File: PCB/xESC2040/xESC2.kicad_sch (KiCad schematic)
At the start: 52 parts, among them J1 Conn_01x06_Male, J2 U254-051T-4BH83-F1S, J3 Conn_01x05_Male, J4 Conn_01x05_Male, J5 Conn_01x03_Male, U1 SN65HVD232

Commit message: WIP new power stage
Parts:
- removed C1, C10, C4, C7, C8, C9: DNP, Capacitor_SMD:C_0603_1608Metric, symbol Device:C
- removed R1, R10, R14, R17, R19, R4: 1k5, Resistor_SMD:R_0603_1608Metric, symbol Device:R
- removed R11, R2, R5: 2k2, Resistor_SMD:R_0603_1608Metric, symbol Device:R
- removed R13, R16, R18: 22k, Resistor_SMD:R_0603_1608Metric, symbol Device:R
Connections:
- net MCU/MISO_EXT renamed MCU/SHUTDOWN
- net MCU/RX_NCS_EXT renamed MCU/UART_RX
- net MCU/SCK_EXT: no longer names the net of J4.3 (Pin_3)
- net MCU/TX_MOSI_EXT renamed MCU/UART_TX
- no-connect marks 1 -> 2
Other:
- sheet MCU ports: added CURRENT_SENSE, SHUTDOWN, UART_RX, UART_TX; removed CUR_U, CUR_V, CUR_W, DRV_ENABLE, DRV_MISO, DRV_MOSI, DRV_NCS, DRV_SCK, FAULT, MISO_EXT, PHASE_U, PHASE_V, PHASE_W, RX_NCS_EXT, SCK_EXT, SERVO, TX_MOSI_EXT
- sheet Power ports: added CUR_SENSE; removed CURU_5V, CURV_5V, CURW_5V, DRV_ENABLE, FAULT, MISO, MOSI, NCS, PHASE_U, PHASE_V, PHASE_W, SCK, VCCIO

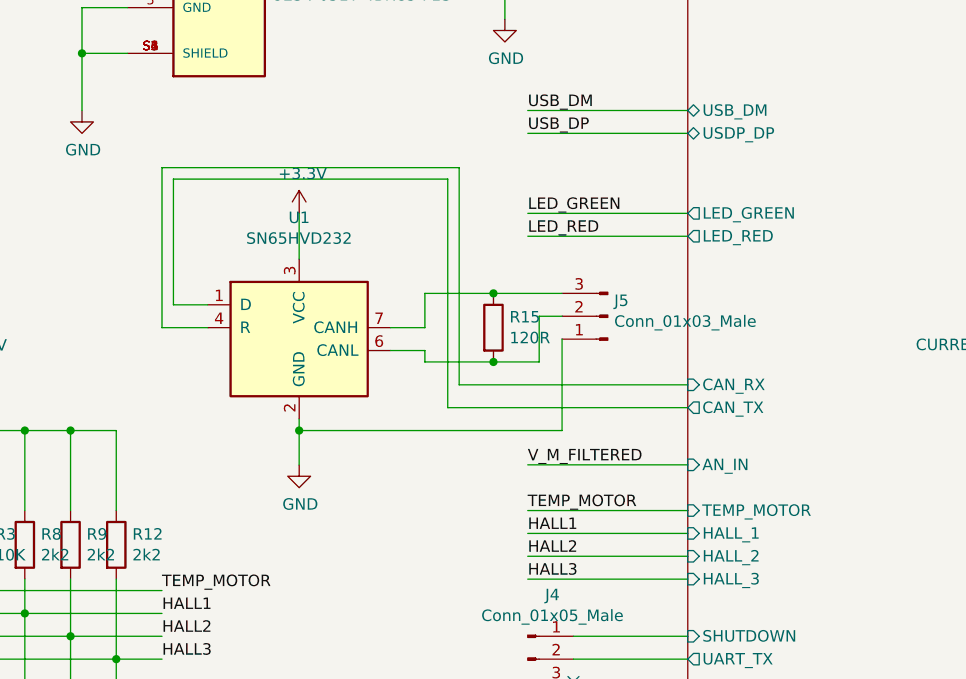
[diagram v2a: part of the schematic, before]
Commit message: added CAN, WIP
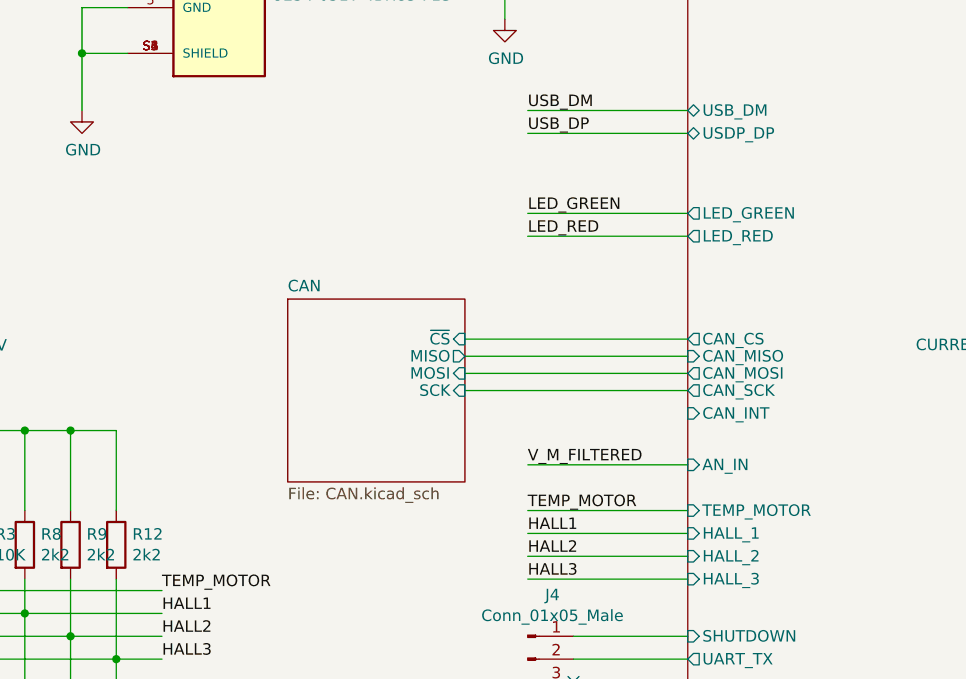
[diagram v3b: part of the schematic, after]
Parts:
- removed J5: Conn_01x03_Male, Connector_PinHeader_2.54mm:PinHeader_1x03_P2.54mm_Vertical, symbol Connector:Conn_01x03_Male
- removed R15: 120R, Resistor_SMD:R_0603_1608Metric, symbol Device:R
- removed U1: SN65HVD232, Package_SO:SOIC-8_3.9x4.9mm_P1.27mm, symbol Interface_CAN_LIN:SN65HVD232
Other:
- added sheet CAN (CAN.kicad_sch)
- sheet MCU ports: added CAN_CS, CAN_INT, CAN_MISO, CAN_MOSI, CAN_SCK; removed CAN_RX, CAN_TX

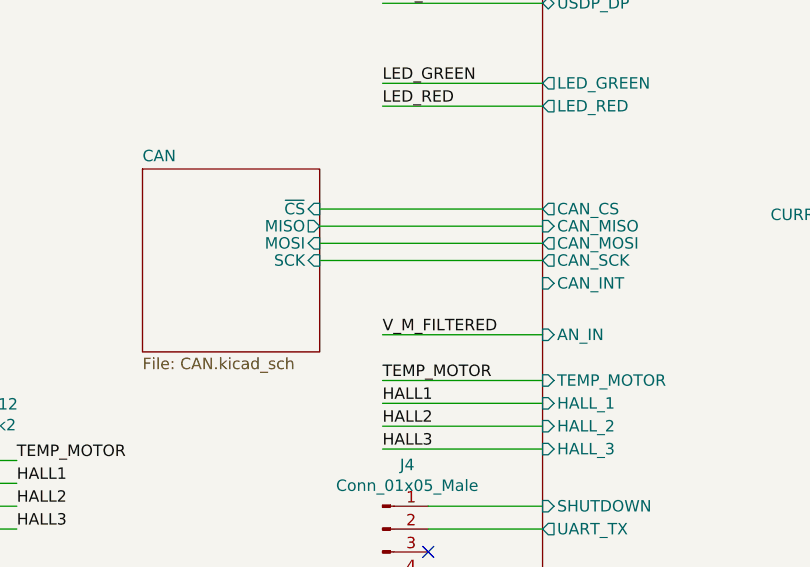
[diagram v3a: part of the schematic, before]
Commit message: added interrupt pin, added vias to the shunt, moved some stuff
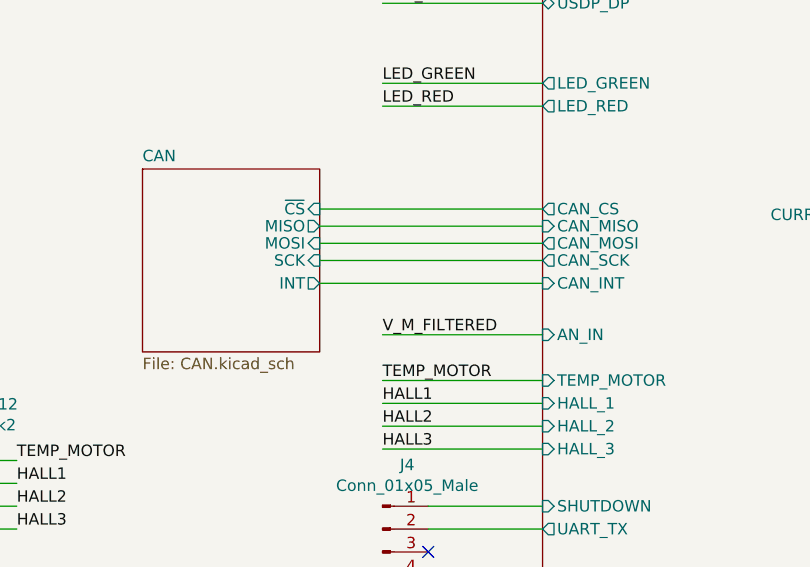
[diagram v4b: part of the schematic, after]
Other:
- sheet CAN ports: added INT; removed none
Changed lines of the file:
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@@
+    (stroke (width 0) (type default) (color 0 0 0 0))
+  )
+  (wire (pts (xy 90.805 93.345) (xy 115.57 93.345))
     (stroke (width 0) (type default) (color 0 0 0 0))
   )
@@
       (effects (font (size 1.27 1.27)) (justify right))
     )
+    (pin "INT" output (at 90.805 93.345 0)
+      (effects (font (size 1.27 1.27)) (justify right))
+    )

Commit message: Added Config field for KiBoM compatability
Added Config field so with and without CAN BoM's can be generated with KiBoM
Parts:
- C3, C5, C6, FID1, FID2, FID3, FID4, FID5, FID6, FID7, FID8: Config (none) -> do not place
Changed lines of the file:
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@@
+      (effects (font (size 1.27 1.27)) hide)
+    )
+    (property "Config" "do not place" (id 4) (at 52.07 127 0)
       (effects (font (size 1.27 1.27)) hide)
     )
@@
       (effects (font (size 1.27 1.27)) hide)
     )
+    (property "Config" "do not place" (id 4) (at 46.99 127 0)
+      (effects (font (size 1.27 1.27)) hide)
+    )
     (pin "1")
     (pin "2")
@@
     )
     (property "Datasheet" "~" (id 3) (at 41.91 127 0)
+      (effects (font (size 1.27 1.27)) hide)
+    )
+    (property "Config" "do not place" (id 4) (at 41.91 127 0)
       (effects (font (size 1.27 1.27)) hide)
     )
@@
       (effects (font (size 1.27 1.27)) hide)
     )
+    (property "Config" "do not place" (id 4) (at 271.78 82.55 0)
+      (effects (font (size 1.27 1.27)) hide)
+    )
   )
   (symbol (lib_id "Mechanical:Fiducial") (at 271.78 87.63 0) (unit 1)
@@
       (effects (font (size 1.27 1.27)) hide)
     )
+    (property "Config" "do not place" (id 4) (at 271.78 87.63 0)
+      (effects (font (size 1.27 1.27)) hide)
+    )
   )
   (symbol (lib_id "Mechanical:Fiducial") (at 271.78 92.71 0) (unit 1)
@@
       (effects (font (size 1.27 1.27)) hide)
     )
+    (property "Config" "do not place" (id 4) (at 271.78 92.71 0)
+      (effects (font (size 1.27 1.27)) hide)
+    )
   )
   (symbol (lib_id "Mechanical:Fiducial") (at 271.78 97.79 0) (unit 1)
@@
       (effects (font (size 1.27 1.27)) hide)
     )
+    (property "Config" "do not place" (id 4) (at 271.78 97.79 0)
+      (effects (font (size 1.27 1.27)) hide)
+    )
   )
   (symbol (lib_id "Mechanical:Fiducial") (at 265.43 82.55 0) (unit 1)
@@
       (effects (font (size 1.27 1.27)) hide)
     )
+    (property "Config" "do not place" (id 4) (at 265.43 82.55 0)
+      (effects (font (size 1.27 1.27)) hide)
+    )
   )
   (symbol (lib_id "Mechanical:Fiducial") (at 265.43 87.63 0) (unit 1)
@@
       (effects (font (size 1.27 1.27)) hide)
     )
+    (property "Config" "do not place" (id 4) (at 265.43 87.63 0)
+      (effects (font (size 1.27 1.27)) hide)
+    )
   )
   (symbol (lib_id "Mechanical:Fiducial") (at 265.43 92.71 0) (unit 1)
@@
       (effects (font (size 1.27 1.27)) hide)
     )
+    (property "Config" "do not place" (id 4) (at 265.43 92.71 0)
+      (effects (font (size 1.27 1.27)) hide)
+    )
   )
   (symbol (lib_id "Mechanical:Fiducial") (at 265.43 97.79 0) (unit 1)
@@
       (effects (font (size 1.27 1.27)) hide)
     )
+    (property "Config" "do not place" (id 4) (at 265.43 97.79 0)
+      (effects (font (size 1.27 1.27)) hide)
+    )

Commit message: add pn's for header pins - all cheapies from LSCS
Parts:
- J1: LCSC (none) -> C2935912; Part Number (none) -> DZ254R-11-06-63; Stock_PN (none) -> J-TH-1x6-.1
- J3, J4: LCSC (none) -> C2935911; Part Number (none) -> DZ254R-11-05-63; Stock_PN (none) -> J-TH-1x5-.1
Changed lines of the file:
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@@
+      (effects (font (size 1.27 1.27)) hide)
+    )
+    (property "LCSC" "C2935912" (id 4) (at 21.59 115.57 0)
+      (effects (font (size 1.27 1.27)) hide)
+    )
+    (property "Part Number" "DZ254R-11-06-63" (id 5) (at 21.59 115.57 0)
+      (effects (font (size 1.27 1.27)) hide)
+    )
+    (property "Stock_PN" "J-TH-1x6-.1" (id 6) (at 21.59 115.57 0)
       (effects (font (size 1.27 1.27)) hide)
     )
@@
     )
     (property "Datasheet" "~" (id 3) (at 85.09 40.64 0)
+      (effects (font (size 1.27 1.27)) hide)
+    )
+    (property "LCSC" "C2935911" (id 4) (at 85.09 40.64 0)
+      (effects (font (size 1.27 1.27)) hide)
+    )
+    (property "Part Number" "DZ254R-11-05-63" (id 5) (at 85.09 40.64 0)
+      (effects (font (size 1.27 1.27)) hide)
+    )
+    (property "Stock_PN" "J-TH-1x5-.1" (id 6) (at 85.09 40.64 0)
       (effects (font (size 1.27 1.27)) hide)
     )
@@
       (effects (font (size 1.27 1.27)) hide)
     )
+    (property "LCSC" "C2935911" (id 4) (at 97.79 123.19 0)
+      (effects (font (size 1.27 1.27)) hide)
+    )
+    (property "Part Number" "DZ254R-11-05-63" (id 5) (at 97.79 123.19 0)
+      (effects (font (size 1.27 1.27)) hide)
+    )
+    (property "Stock_PN" "J-TH-1x5-.1" (id 6) (at 97.79 123.19 0)
+      (effects (font (size 1.27 1.27)) hide)
+    )
